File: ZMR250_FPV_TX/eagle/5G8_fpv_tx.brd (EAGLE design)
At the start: 50.8 x 30.5 mm, 20 parts, among them X1 LTI-SASF54GT, X2 53048-06, X3 53048-06

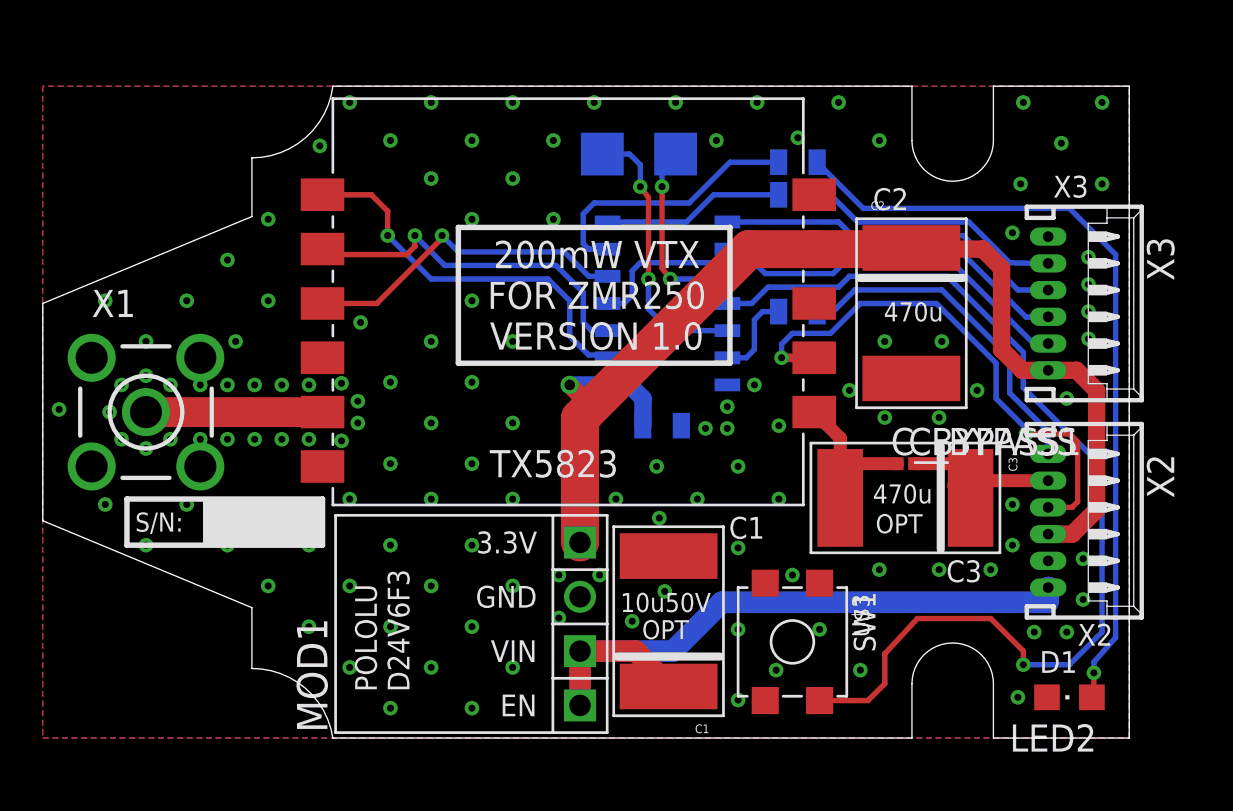
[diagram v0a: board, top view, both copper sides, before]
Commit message: added separate EAGLE directory and updated README and latest board files
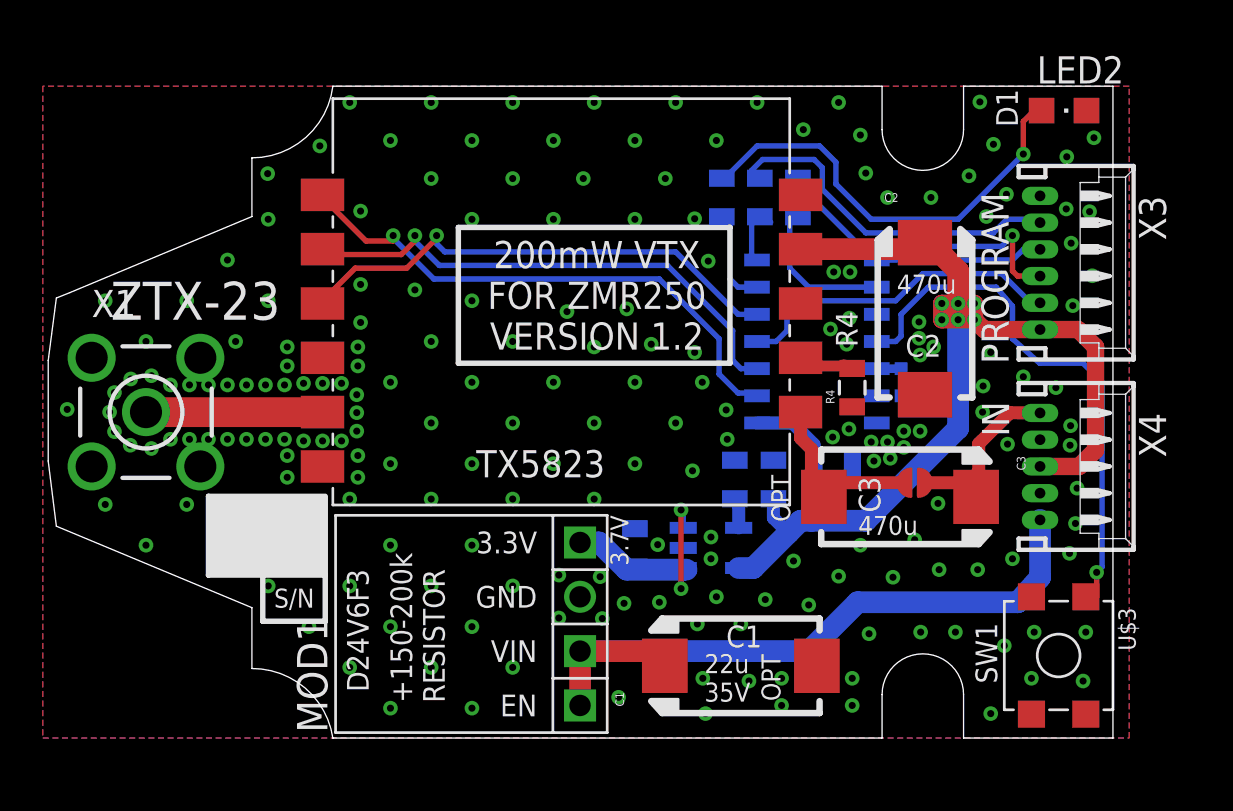
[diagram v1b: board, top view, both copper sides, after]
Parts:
- removed C_BYPASS, C_BYPASS1: TPTP06SQ, testpad:TP06SQ
- removed X2: 53048-06, con-molex:53048-06
- added C5, C6, C7: .1u, SparkFun-Passives:0805
- added SJ1: JS_ROUND, 5G8_fpv:SJ_ROUND
- added U2: REG113NA-3/250, Texas Instruments_By_element14_Batch_1:SOT95P280X145-5N
- added X4: 53048-05, con-molex:53048-05
- TP1, TP2: value TPTP20SQ -> TPTP06SQ; device testpad:TP20SQ -> testpad:TP06SQ
- moved LED2 27.4 mm to (50.3, 33.1), turned to 270 degrees
- moved TP1 17.2 mm to (42.7, 21.1)
- moved TP2 15.5 mm to (42.7, 19.8)
- moved U$3 12.5 mm to (51.3, 10.4)
- moved C4 8.20 mm to (39.5, 16.6)
- moved U$1 7.21 mm to (38.7, 22.4)
- moved R4 4.37 mm to (40.4, 20.2), flipped to the top, turned to 90 degrees
- moved C1 3.97 mm to (35.2, 7.19), turned to 90 degrees
- moved R1 3.92 mm to (34.3, 29.1), turned to 90 degrees
- moved R3 2.41 mm to (37.8, 29.1), turned to 90 degrees
- moved X3 1.94 mm to (50.4, 26.0)
- moved R2 1.78 mm to (36.1, 29.1), turned to 90 degrees
- moved C2 0.68 mm to (43.8, 23.4)
- moved U$2 0.63 mm to (38.0, 19.1)
- moved C3 0.26 mm to (42.6, 15.1)
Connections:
- removed net N$3: LED2.A, R1.2
- removed net RC_IN: R4.1, X2.6
- removed net RC_UC: R4.2, U$1.13
- new net LED_OUT: R1.1, U$1.6
- new net N$1: C5.1, MOD1.O, U2.1, U2.3
- new net N$2: C6.1, U2.4
- new net TP3: U$1.10
- net 3V3: now also C7.1, U2.5, X4.3; no longer MOD1.O, X2.3
- net AUD: now also R4.2; no longer X2.4
- net GND: now also C5.2, C6.2, C7.2, R4.1, U2.2, X4.2, X4.4; no longer X2.2
- net LED: now also LED2.A, R1.2; no longer R1.1, U$1.6
- net SW1: now also U$3.1.2; no longer U$3.1.1
- net TP2: now also U$1.13; no longer U$1.10
- net VBATT: now also X4.1; no longer X2.1
- net VID: now also SJ1.1; no longer C_BYPASS1.TP
- net VID_IN: now also SJ1.2, X4.5; no longer C_BYPASS.TP, X2.5
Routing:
- net N$3: track 36.9 -> 0.00 mm, vias 1 -> 0
- net SW1: track 48.0 -> 25.6 mm
- net AUD: track 24.9 -> 2.63 mm, vias 2 -> 0
- net RC_IN: track 16.0 -> 0.00 mm
- net N$1: track 0.00 -> 12.2 mm, vias 0 -> 2
- net TP1: track 13.0 -> 1.14 mm, vias 2 -> 0
- net TP2: track 8.92 -> 0.00 mm, vias 2 -> 0
- net MISO: track 16.3 -> 8.08 mm
- net SPI_CK: track 15.5 -> 23.5 mm
- net LED: track 12.8 -> 20.6 mm, vias 0 -> 1
- net SPI_EN: track 16.7 -> 24.4 mm
- net SPI_D: track 18.2 -> 25.9 mm
- net RST: track 24.0 -> 16.6 mm
- net MOSI: track 8.52 -> 3.04 mm
- net 3V3: track 53.9 -> 58.8 mm, vias 1 -> 6
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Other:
- board size 50.8 x 30.5 mm -> 49.8 x 30.5 mm
- board text added: "+150-200k RESISTOR"
- board text added: "200mW VTX FOR ZMR250 VERSION 1.2"
- board text added: "22u 35V"
- board text added: "25MAY15"
- board text added: "3.7V"
- board text added: "C5"
- board text added: "C6"
- board text added: "C7"
- board text added: "D24V6F3"
- board text added: "GND MO MI SC RST 3V3"
- board text added: "IN"
- board text added: "INPUT"
- board text added: "PROGRAM"
- board text added: "S/N"
- board text added: "SMA"
- board text added: "U2"
- board text added: "VID GND 3.3V GND BATT"
- board text added: "ZTX-23"
- board text removed: "10u50V"
- board text removed: "11APR15"
- board text removed: "200mW VTX FOR ZMR250 VERSION 1.0"
- board text removed: "CTL VID AUD 3.3V GND BATT"
- board text removed: "GND MOSI MISO SCL RST 3.3V"
- board text removed: "POLOLU D24V6F3"
- board text removed: "S/N:"
- board text removed: "TP1"
- board text removed: "TP2"
- board text removed: "X1"
- board text removed: "X2"
- board text removed: "X3"
